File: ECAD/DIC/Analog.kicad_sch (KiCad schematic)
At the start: 28 parts, among them Q1 2N7002, Q2 2N7002, Q3 2N7002, Q4 2N7002

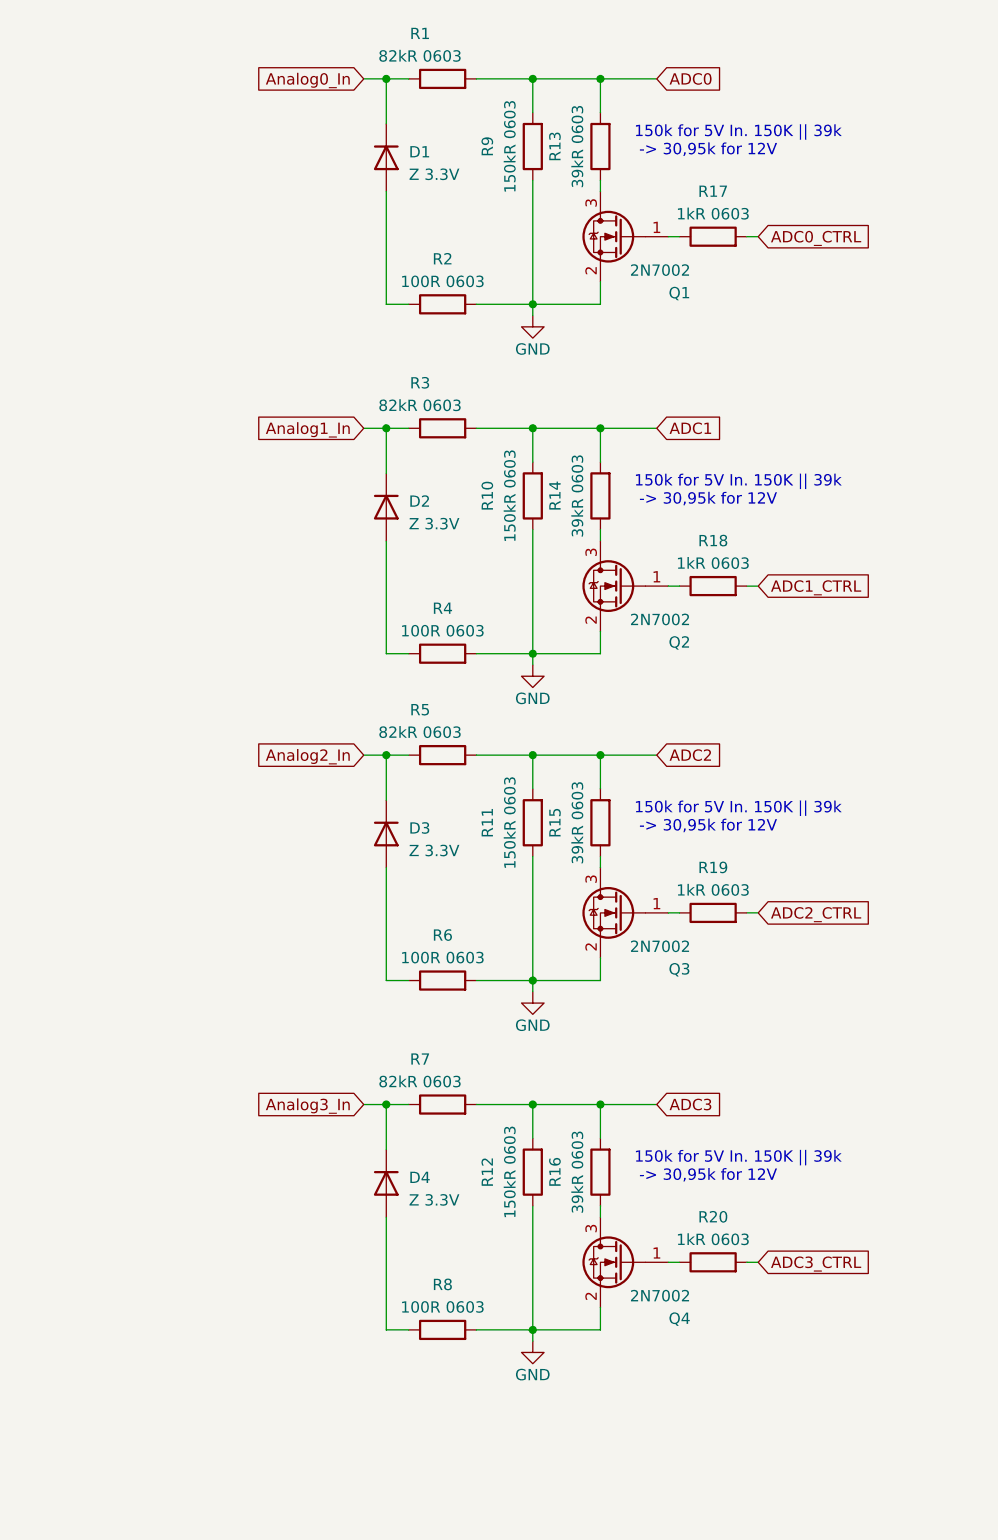
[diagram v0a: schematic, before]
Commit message: Finish Schematic for V3 PCB
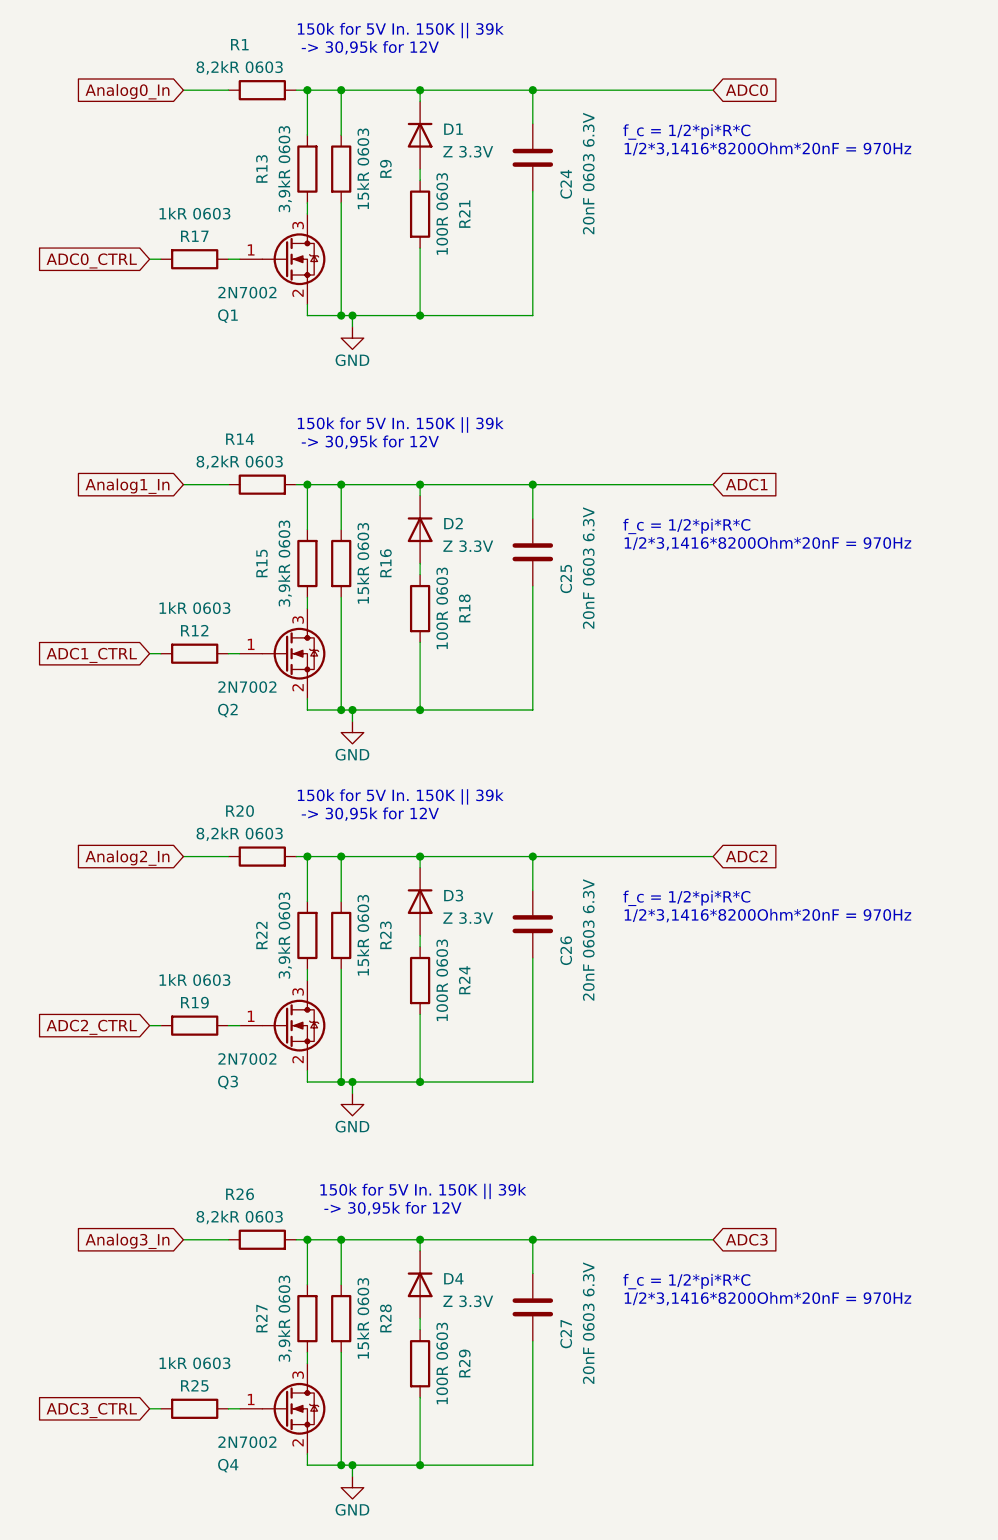
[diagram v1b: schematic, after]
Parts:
- removed R10, R11: 150kR 0603, Resistor_SMD:R_0603_1608Metric_Pad0.98x0.95mm_HandSolder, symbol Device:R
- removed R2, R4, R6, R8: 100R 0603, Resistor_SMD:R_0603_1608Metric_Pad0.98x0.95mm_HandSolder, symbol Device:R
- removed R3, R5, R7: 82kR 0603, Resistor_SMD:R_0603_1608Metric_Pad0.98x0.95mm_HandSolder, symbol Device:R
- added C24, C25, C26, C27: 20nF 0603 6.3V, Capacitor_SMD:C_0603_1608Metric_Pad1.08x0.95mm_HandSolder, symbol Device:C
- added R21, R24, R29: 100R 0603, Resistor_SMD:R_0603_1608Metric_Pad0.98x0.95mm_HandSolder, symbol Device:R
- added R22, R27: 3,9kR 0603, Resistor_SMD:R_0603_1608Metric_Pad0.98x0.95mm_HandSolder, symbol Device:R
- added R23, R28: 15kR 0603, Resistor_SMD:R_0603_1608Metric_Pad0.98x0.95mm_HandSolder, symbol Device:R
- added R25: 1kR 0603, Resistor_SMD:R_0603_1608Metric_Pad0.98x0.95mm_HandSolder, symbol Device:R
- added R26: 8,2kR 0603, Resistor_SMD:R_0603_1608Metric_Pad0.98x0.95mm_HandSolder, symbol Device:R
- R1: value 82kR 0603 -> 8,2kR 0603
- R12: value 150kR 0603 -> 1kR 0603
- R13, R15: value 39kR 0603 -> 3,9kR 0603
- R14: value 39kR 0603 -> 8,2kR 0603
- R16: value 39kR 0603 -> 15kR 0603
- R18: value 1kR 0603 -> 100R 0603
- R20: value 1kR 0603 -> 8,2kR 0603
- R9: value 150kR 0603 -> 15kR 0603
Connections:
- net ADC0: now also D1.1 (K), R9.1, C24.2; no longer R9.2
- net ADC1: now also D2.1 (K), R15.2, R16.1, C25.2
- net ADC1_CTRL: now also R12.2; no longer R18.2
- net ADC2: now also D3.1 (K), R20.2, C26.2, R22.2, R23.1; no longer R15.2
- net ADC3: now also D4.1 (K), C27.2, R26.2, R27.2, R28.1; no longer R12.2, R16.2
- net ADC3_CTRL: now also R25.2; no longer R20.2
- net Analog0_In: no longer D1.1 (K)
- net Analog1_In: now also R14.1; no longer D2.1 (K)
- net Analog2_In: now also R20.1; no longer D3.1 (K)
- net Analog3_In: now also R26.1; no longer D4.1 (K)
- net GND: now also R16.2, R18.2, R9.2, C24.1, C25.1, C26.1, C27.1, R21.2, R23.2, R24.2, R28.2, R29.2; no longer R12.1, R9.1
- net at Q4.3 (D): now also R27.1; no longer R16.1
- net at Q2.1 (G): now also R12.1; no longer R18.1
- net at D3.2 (A): now also R24.1
- net at Q2.3 (D): now also R15.1; no longer R14.1
- net at D4.2 (A): now also R29.1
- net at D2.2 (A): now also R18.1
- net at D1.2 (A): now also R21.1
- net at Q4.1 (G): now also R25.1; no longer R20.1
- net at Q3.3 (D): now also R22.1; no longer R15.1
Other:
- note added: "f_c = 1/2*pi*R*C 1/2*3,1416*8200Ohm*20nF = 970Hz"
- moved on the sheet: R1, R9

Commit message: switch to ribbon cable pcb interconnect
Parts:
- removed C24, C25: 20nF 0603 6.3V, Capacitor_SMD:C_0603_1608Metric_Pad1.08x0.95mm_HandSolder, symbol Device:C
- removed D1, D2, D3, D4: Z 3.3V, Diode_SMD:D_SOD-323_HandSoldering, symbol Device:D
- removed Q1, Q2, Q3, Q4: 2N7002, Package_TO_SOT_SMD:SOT-23, symbol Transistor_FET:2N7002
- removed R1, R14, R20: 8,2kR 0603, Resistor_SMD:R_0603_1608Metric_Pad0.98x0.95mm_HandSolder, symbol Device:R
- removed R12, R19, R25: 1kR 0603, Resistor_SMD:R_0603_1608Metric_Pad0.98x0.95mm_HandSolder, symbol Device:R
- removed R15, R22, R27: 3,9kR 0603, Resistor_SMD:R_0603_1608Metric_Pad0.98x0.95mm_HandSolder, symbol Device:R
- removed R16, R23, R28, R9: 15kR 0603, Resistor_SMD:R_0603_1608Metric_Pad0.98x0.95mm_HandSolder, symbol Device:R
- removed R18, R21, R24, R29: 100R 0603, Resistor_SMD:R_0603_1608Metric_Pad0.98x0.95mm_HandSolder, symbol Device:R
- added C29: 160nF 0603 6.3V, Capacitor_SMD:C_0603_1608Metric_Pad1.08x0.95mm_HandSolder, symbol Device:C
- added C30, C31: 100nF 0603 6.3V, Capacitor_SMD:C_0603_1608Metric_Pad1.08x0.95mm_HandSolder, symbol Device:C
- added D10: Z 3.3V, Diode_SMD:D_SOD-323_HandSoldering, symbol Device:D
- added D8: NSVRB751V40T1G, Diode_SMD:D_SOD-323_HandSoldering, symbol Device:D_Schottky
- added Q1, Q7: BC846, Package_TO_SOT_SMD:SOT-23, symbol Transistor_BJT:BC846
- added R31: 100 0603, Resistor_SMD:R_0603_1608Metric_Pad0.98x0.95mm_HandSolder, symbol Device:R
- added R34: 1k 0603 0.1%, Resistor_SMD:R_0603_1608Metric_Pad0.98x0.95mm_HandSolder, symbol Device:R
- added R36: 100 0603 0.1%, Resistor_SMD:R_0603_1608Metric_Pad0.98x0.95mm_HandSolder, symbol Device:R
- added R38: 82kR 0603 0.1%, Resistor_SMD:R_0603_1608Metric_Pad0.98x0.95mm_HandSolder, symbol Device:R
- added R39: 39kR 0603 0.1%, Resistor_SMD:R_0603_1608Metric_Pad0.98x0.95mm_HandSolder, symbol Device:R
- added R40: 150kR 0603 0.1%, Resistor_SMD:R_0603_1608Metric_Pad0.98x0.95mm_HandSolder, symbol Device:R
- added U10, U9: ADA4500-2, Package_SO:MSOP-8_3x3mm_P0.65mm, symbol Device:Opamp_Dual
- C26, C27: value 20nF 0603 6.3V -> 10uF 0805 6.3V; footprint Capacitor_SMD:C_0603_1608Metric_Pad1.08x0.95mm_HandSolder -> Capacitor_SMD:C_0805_2012Metric_Pad1.18x1.45mm_HandSolder
- R13: value 3,9kR 0603 -> 100 0603
- R17: value 1kR 0603 -> 5kR 0603 0.1%
- R26: value 8,2kR 0603 -> 2.2MR 0603 0.1%
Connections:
- net ADC2 is gone; now on net GND: C26.2
- net ADC0: now also C29.2, R36.2; no longer R13.2
- net ADC0_CTRL: now also R31.2; no longer R17.2
- net Analog0_In: now also R17.2, R38.1
- net GND: now also C29.1, C30.1, C31.2, D10.2 (A), Q1.2 (E), Q7.2 (E), R34.1, R40.2, U10.4 (V-), U9.4 (V-); no longer C26.1
- net at R13.1: now also Q1.1 (B)
- net at R17.1: now also Q1.3 (C)
- net ADC3: no longer names the net of R26.2
- net ADC3: now also R38.2, R39.2, R40.1, U10.3 (+); no longer C27.2
- net Analog3_In renamed +3.3V
- net +3.3V: now also D10.1 (K), D8.1 (K)
- new net: D8.2 (A), R34.2, R36.1, U10.1, U10.2 (-)
- new net: Q7.1 (B), R31.1
- new net: Q7.3 (C), R39.1
- new net +5V: C26.1, C27.2, C30.2, C31.1, U10.8 (V+), U9.8 (V+)
- new net ADC0_NTC_CTRL: R13.2
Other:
- note added: "10k NTC Complement = 5K for highest delta from 0-100°C PT1000 Complement = 1150 for highest delta from 0-100°C PT100 Complement = 115 for highest delta from 0-100°C"
- note added: "ADA4500"
- note added: "Abweichung durch belasteten SPannungsteiler so groß, das Dimensionierung der Eingangsimoedanz in bezug auf andere Abweichungsmechanismen nicht praktikabel -> Auswertung von Potis in SW nur über belasteten SPannungsteiler"
- note added: "Additional ZDiode against 3.3V Overload"
- note added: "Analog Front End for Sensors with Generic 5V and 12V Output Potentiometers NTC and PTC's For Ratiometric Sensing use second Analogue Input for Supply Sensing Up to 1kHz of Data Output and with 12Bit resolution and ~2mV Precision"
- note added: "CB Cutoff current -> 15nA over 39kOhm -> 0,585mV"
- note added: "Fehler durch belasteten spannungsteiler idr so groß das ohne impedanzwandler nicht praktikabel. Eingangsimpedanz muss bei 500k und größer liegen damit der Messfehler hinreichend klein wird. -> Bei Poti, berechung des Eingangswertes nur über belasteten spannungsteiler!!!"
- note added: "Input Offset Current = 170pA over max. 150kOhm -> 0,0255mV"
- note added: "Opamp Realistically capable of driving in a range of 40mV - 4.95V Max Voltage around 3.3V Introduce Voltage offset to avoid clipping at min level"
- note added: "Overvoltage Protection I_R (D1) = max 2uA -> Sim I_R < 200nA U_R1_Error = 1kOhm * 2uA = 2mV max. probably more like -> 0,2mV"
- note added: "Pulldown to drain Overvoltage Protection diode leackage current"
- note added: "RC-Filter f_c = 1/(2*pi*R*C) 1/2*3,1416*100Ohm*160nF = 9947Hz -> 10khz due to very broad influence of filter Max Signal Frequency expected 1kHz Signal Processing with 10Khz or more and FIR Filter buildup of -100db from 1-10khz"
- note added: "Switchable Voltage Divider 150k for 5V & 150K || 39k -> 30,95k for 12V 5V -> (82k -- 150k) = 3,2328V 12V -> (82k -- 30.95k) = 3,2882V with 0.1% worst case = 3,2350V -> +-2,2mV error"
- note added: "To ADC, 12Bit Resolution = 0,81mV LSB"
- note added: "Voltage Offset to Avoid clipping on ADC Input Only Applicabale for open NTC CTRL @30.95k -> 45.75mV @150k -> 210.64mV @30.95k and closed NTC CTRL -> 26.93k -> 35.51mV"
- note removed: "150k for 5V In. 150K || 39k -> 30,95k for 12V"
- note removed: "f_c = 1/2*pi*R*C 1/2*3,1416*8200Ohm*20nF = 970Hz"

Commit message: few small changes
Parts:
- added R57: 10kR 0603, Resistor_SMD:R_0603_1608Metric_Pad0.98x0.95mm_HandSolder, symbol Device:R
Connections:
- net +3.3V: now also R57.1
- net ADC0_CTRL: now also R57.2
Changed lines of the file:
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@@
   (junction (at 264.16 26.67) (diameter 0) (color 0 0 0 0)
   )
+  (junction (at 97.79 146.05) (diameter 0) (color 0 0 0 0)
+  )
   (junction (at 227.33 26.67) (diameter 0) (color 0 0 0 0)
   )
@@
   (junction (at 152.4 93.98) (diameter 0) (color 0 0 0 0)
   )
+  (wire (pts (xy 92.71 148.59) (xy 92.71 146.05))
+    (stroke (width 0) (type default))
+  )
   (wire (pts (xy 85.09 91.44) (xy 92.71 91.44))
     (stroke (width 0) (type default))
@@
     (stroke (width 0) (type default))
   )
-  (wire (pts (xy 97.79 147.32) (xy 97.79 144.78))
+  (wire (pts (xy 97.79 147.32) (xy 97.79 146.05))
     (stroke (width 0) (type default))
   )
@@
     (stroke (width 0) (type default))
   )
+  (wire (pts (xy 92.71 146.05) (xy 97.79 146.05))
+    (stroke (width 0) (type default))
+  )
   (wire (pts (xy 238.76 26.67) (xy 238.76 27.94))
     (stroke (width 0) (type default))
@@
     (stroke (width 0) (type default))
   )
+  (wire (pts (xy 97.79 146.05) (xy 97.79 144.78))
+    (stroke (width 0) (type default))
+  )
   (wire (pts (xy 97.79 137.16) (xy 97.79 125.73))
     (stroke (width 0) (type default))
@@
         )
       )
+    )
+  )
+  (symbol (lib_id "power:+3.3V") (at 92.71 156.21 180) (unit 1)
+    (in_bom yes) (on_board yes) (dnp no) (fields_autoplaced)
+    (property "Reference" "#PWR065" (at 92.71 152.4 0)
+      (effects (font (size 1.27 1.27)) hide)
+    )
+    (property "Value" "+3.3V" (at 92.71 161.29 0)
+      (effects (font (size 1.27 1.27)))
+    )
+    (property "Footprint" "" (at 92.71 156.21 0)
+      (effects (font (size 1.27 1.27)) hide)
+    )
+    (property "Datasheet" "" (at 92.71 156.21 0)
+      (effects (font (size 1.27 1.27)) hide)
+    )
+    (pin "1")
+    (instances
+      (project "DIC"
+        (path "/64369a6c-13db-47f8-8de7-12b4f0b9bc27/f6b69984-9dac-43ef-98a3-3052766f7d30"
+          (reference "#PWR065") (unit 1)
+        )
+      )
+    )
+  )
+  (symbol (lib_id "Device:R") (at 92.71 152.4 180) (unit 1)
+    (in_bom yes) (on_board yes) (dnp no)
+    (property "Reference" "R57" (at 92.71 152.4 90)
+      (effects (font (size 1.27 1.27)))
+    )
+    (property "Value" "10kR 0603" (at 90.17 152.4 90)
+      (effects (font (size 1.27 1.27)))
+    )
+    (property "Footprint" "Resistor_SMD:R_0603_1608Metric_Pad0.98x0.95mm_HandSolder" (at 94.488 152.4 90)
+      (effects (font (size 1.27 1.27)) hide)
+    )
+    (property "Datasheet" "~" (at 92.71 152.4 0)
+      (effects (font (size 1.27 1.27)) hide)
+    )
+    (pin "1")
+    (pin "2")
+    (instances
+      (project "DIC"
+        (path "/64369a6c-13db-47f8-8de7-12b4f0b9bc27/f6b69984-9dac-43ef-98a3-3052766f7d30"
+          (reference "R57") (unit 1)
+        )
+      )
